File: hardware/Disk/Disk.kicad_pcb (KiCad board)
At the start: 2 copper layers, 95 x 95 mm, 1 part

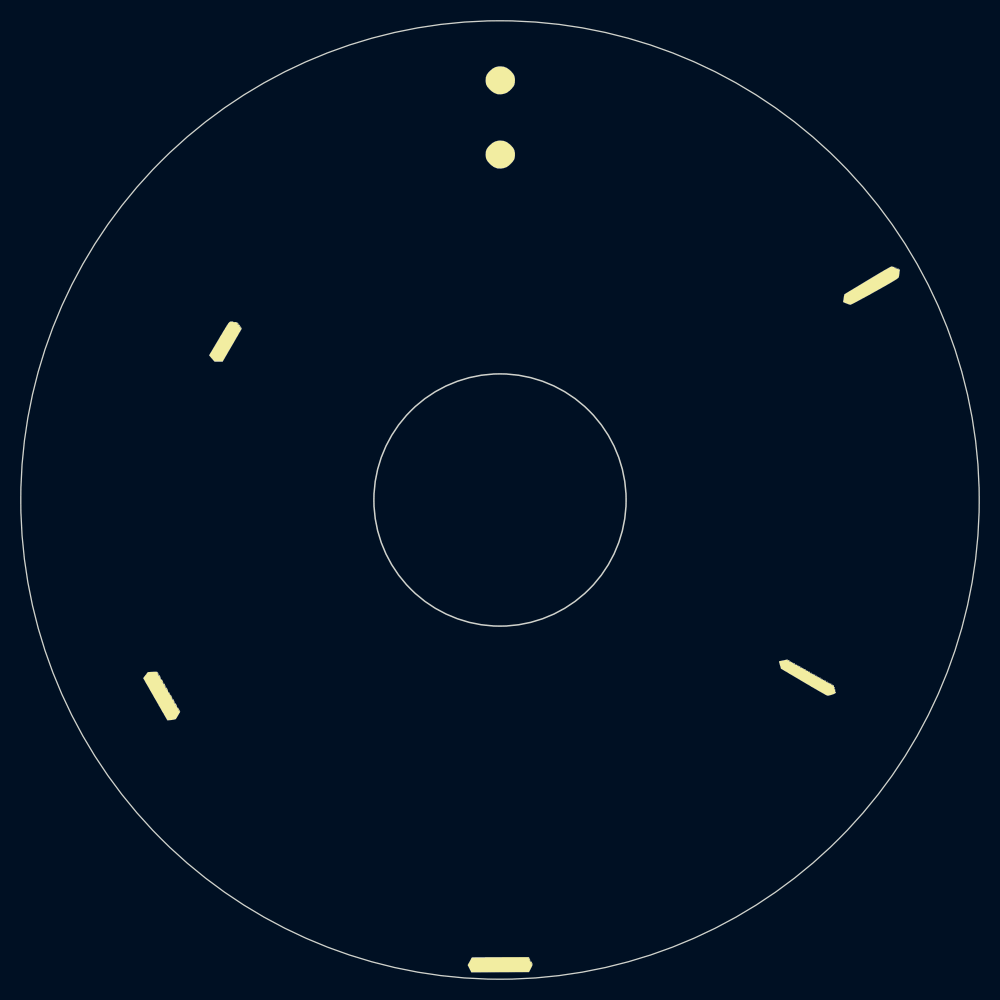
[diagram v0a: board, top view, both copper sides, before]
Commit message: Some changes to disk pattern
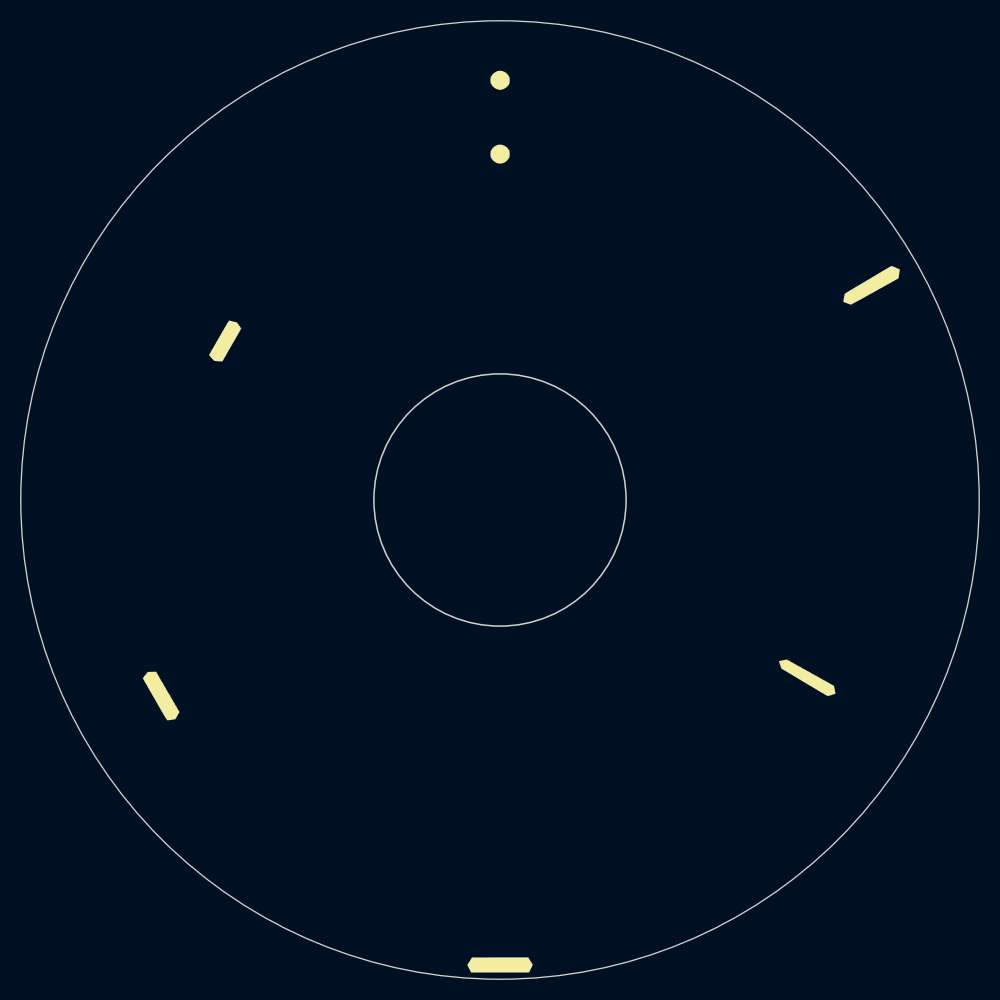
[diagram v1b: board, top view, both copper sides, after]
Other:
- board text added: "Bottom"
- board text added: "Nerd Clock Face 2136A Tom Wimmenhove"
